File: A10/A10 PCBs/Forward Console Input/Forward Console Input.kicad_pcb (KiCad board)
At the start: 2 copper layers, 99.7 x 98.4 mm, 68 parts, among them J1 PATCH, J10 ROWS, J11 COLUMNS, J12 PATCH, J13 PATCH, J14 PWM, J15 PWM, J16 Communication, J17 PATCH, J18 PATCH, J19 PATCH, J2 FIRE HANDLES, J20 PATCH, J21 Analog, J22 Analog, J23 PATCH, J24 PATCH, J25 Power, J26 Power, J27 Analog, J28 Analog, J29 Digital, J3 UFC COLS, J30 PWM, J31 PWM, J32 Communication, J4 UFC ROWS, J5 PATCH, J6 JAMMER, J7 LANDING GEAR, J8 MASTER ARM, J9 NMSP CMSP, U1 USR-ES1

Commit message: A10
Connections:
- R1 pad 1: /*5 -> /*13
- R2 pad 1: /*6 -> /*12
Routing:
- net GND: track 205.5 -> 0.00 mm
- net /39: track 155.7 -> 0.00 mm
- net /38: track 148.8 -> 0.00 mm
- net /43: track 139.9 -> 0.00 mm, vias 2 -> 0
- net /40: track 139.5 -> 0.00 mm
- net /42: track 122.0 -> 0.00 mm, vias 1 -> 0
- net +5V: track 115.4 -> 0.00 mm
- net /32: track 110.1 -> 0.00 mm, vias 1 -> 0
- net /41: track 107.7 -> 0.00 mm
- net MOSI: track 96.1 -> 0.00 mm
- net /33: track 92.5 -> 0.00 mm, vias 1 -> 0
- net SCLK: track 85.4 -> 0.00 mm
- net /34: track 82.3 -> 0.00 mm, vias 3 -> 0
- net SS: track 80.5 -> 0.00 mm
- net ES1_RST: track 78.1 -> 0.00 mm
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
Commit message: a10
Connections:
- C13 pad 1: /A3 -> /A8
- J2 pad 3: /ROW1O -> /32
- J22 pad 1: /A3 -> /A8
- J28 pad 1: /A3 -> /A8
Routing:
- net GND: track 0.00 -> 214.8 mm
- net /38: track 0.00 -> 154.7 mm
- net /39: track 0.00 -> 153.3 mm, vias 0 -> 1
- net /40: track 0.00 -> 126.4 mm, vias 0 -> 1
- net /41: track 0.00 -> 121.0 mm, vias 0 -> 1
- net /43: track 0.00 -> 119.2 mm, vias 0 -> 3
- net /34: track 0.00 -> 118.3 mm, vias 0 -> 1
- net +5V: track 0.00 -> 116.3 mm
- net /33: track 0.00 -> 100.5 mm, vias 0 -> 2
- net MOSI: track 0.00 -> 97.4 mm
- net /32: track 0.00 -> 94.5 mm
- net /42: track 0.00 -> 94.3 mm, vias 0 -> 1
- net SCLK: track 0.00 -> 84.9 mm
- net SS: track 0.00 -> 80.5 mm
- net ES1_RST: track 0.00 -> 77.6 mm
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
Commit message: A10
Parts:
- J7: footprint Connector_Molex:Molex_KK-254_AE-6410-06A_1x06_P2.54mm_Vertical -> Connector_Molex:Molex_KK-254_AE-6410-08A_1x08_P2.54mm_Vertical
- moved J7 1.37 mm to (193.7, 122.4)
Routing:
- net /37: track 21.8 -> 68.2 mm, vias 0 -> 3
- net /41: track 121.0 -> 153.2 mm
- net /34: track 118.3 -> 89.2 mm, vias 1 -> 3
- net /36: track 56.4 -> 77.0 mm
- net /39: track 153.3 -> 135.5 mm
- net /38: track 154.7 -> 140.5 mm
- net /33: track 100.5 -> 89.2 mm, vias 2 -> 0
- net /*45: track 53.8 -> 62.8 mm, vias 1 -> 2
- net /32: track 94.5 -> 103.4 mm
- net /43: track 119.2 -> 125.4 mm, vias 3 -> 1
- net /28: track 58.7 -> 62.9 mm
- net /22: track 53.9 -> 49.8 mm
- net +5V: track 116.3 -> 120.3 mm, vias 0 -> 2
- net /23: track 50.8 -> 47.2 mm
- net /24: track 47.5 -> 44.1 mm
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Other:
- board text added: "A10 FORWARD CONSOLE VER 1.1"
- board text removed: "A10 FORWARD CONSOLE VER 1.0"

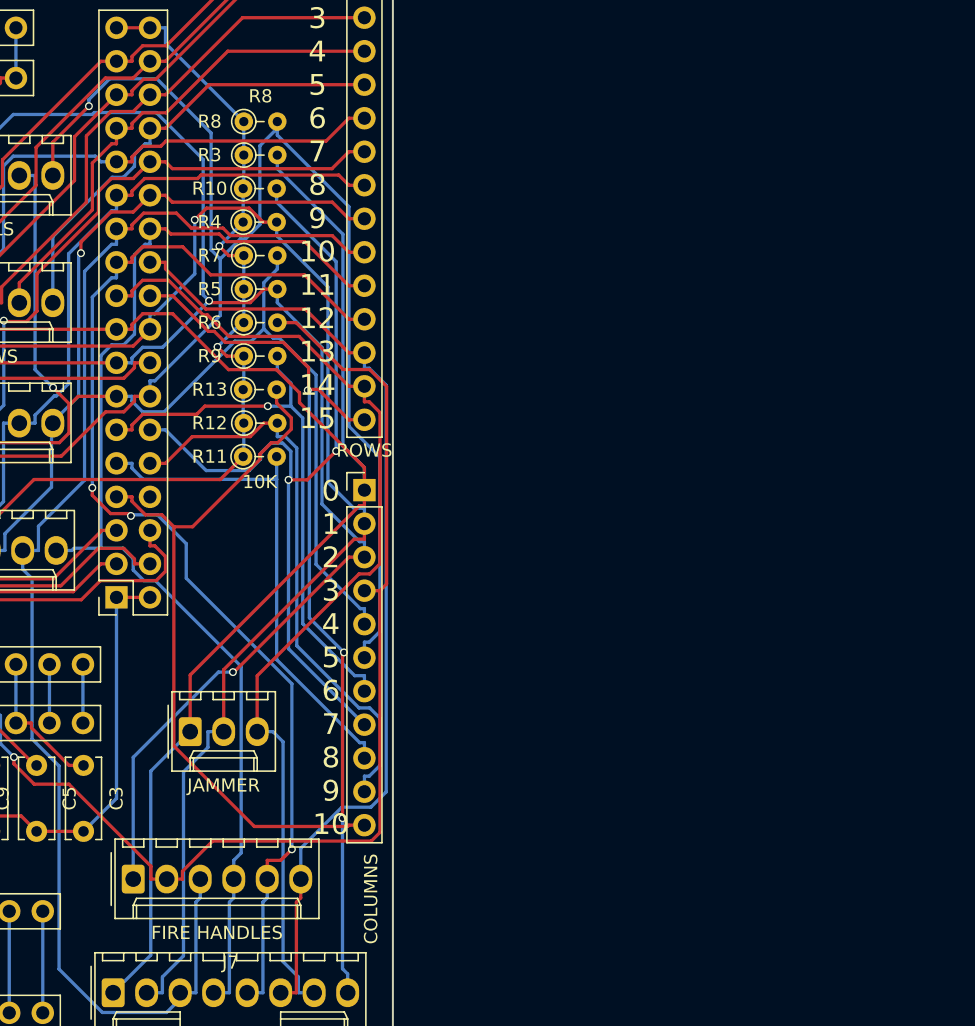
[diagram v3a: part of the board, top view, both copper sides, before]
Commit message: A10 FORWARD INPUT PCB
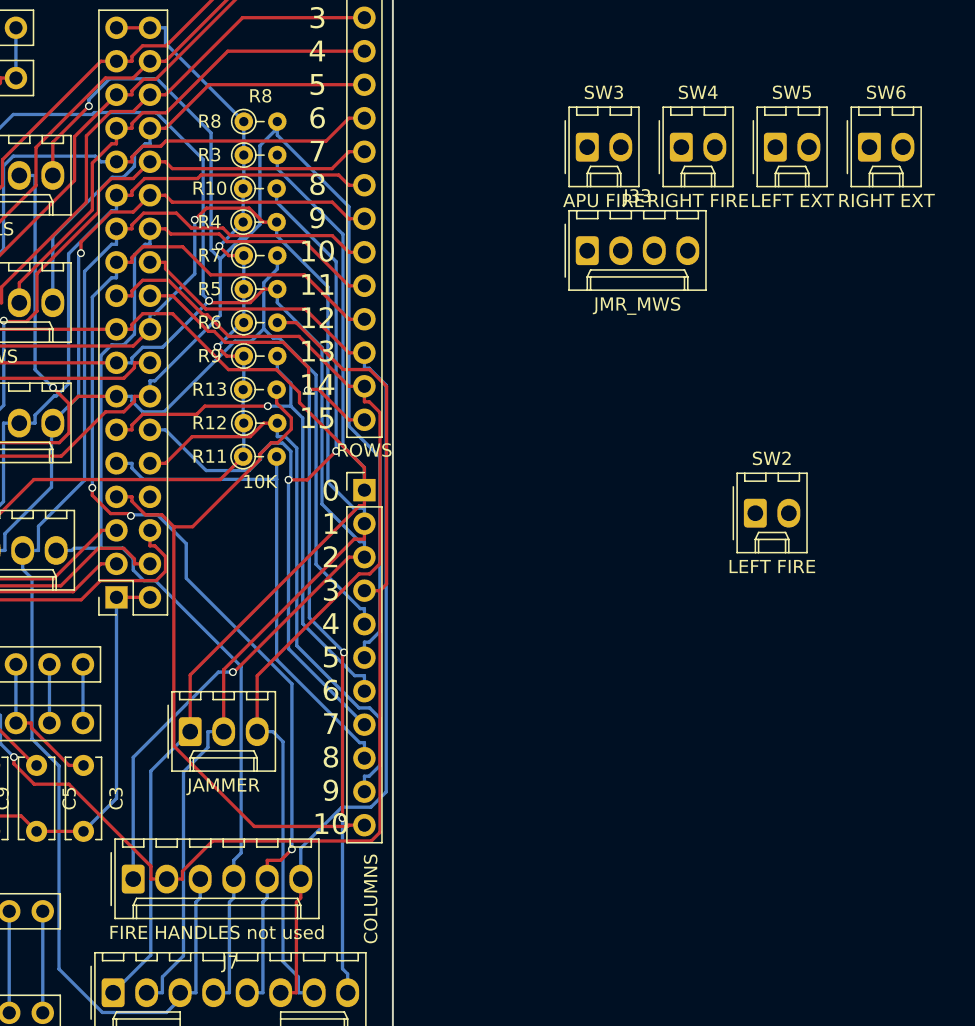
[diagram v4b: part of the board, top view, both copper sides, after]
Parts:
- added J33: JMR_MWS, Connector_Molex:Molex_KK-254_AE-6410-04A_1x04_P2.54mm_Vertical, F.Cu at (229.7, 66.1)
- added SW2: LEFT FIRE, Connector_Molex:Molex_KK-254_AE-6410-02A_1x02_P2.54mm_Vertical, F.Cu at (242.4, 86.0)
- added SW3: APU FIRE, Connector_Molex:Molex_KK-254_AE-6410-02A_1x02_P2.54mm_Vertical, F.Cu at (229.7, 58.2)
- added SW4: RIGHT FIRE, Connector_Molex:Molex_KK-254_AE-6410-02A_1x02_P2.54mm_Vertical, F.Cu at (236.8, 58.2)
- added SW5: LEFT EXT, Connector_Molex:Molex_KK-254_AE-6410-02A_1x02_P2.54mm_Vertical, F.Cu at (243.9, 58.2)
- added SW6: RIGHT EXT, Connector_Molex:Molex_KK-254_AE-6410-02A_1x02_P2.54mm_Vertical, F.Cu at (251.1, 58.2)
- J2: value FIRE HANDLES -> FIRE HANDLES not used
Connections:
- J29 pad 11: /*44 -> unconnected-(J29-Pin_11-Pad11)
- J29 pad 13: /42 -> unconnected-(J29-Pin_13-Pad13)
- J29 pad 27: /28 -> unconnected-(J29-Pin_27-Pad27)
- J29 pad 31: /24 -> unconnected-(J29-Pin_31-Pad31)
- J29 pad 33: /22 -> unconnected-(J29-Pin_33-Pad33)

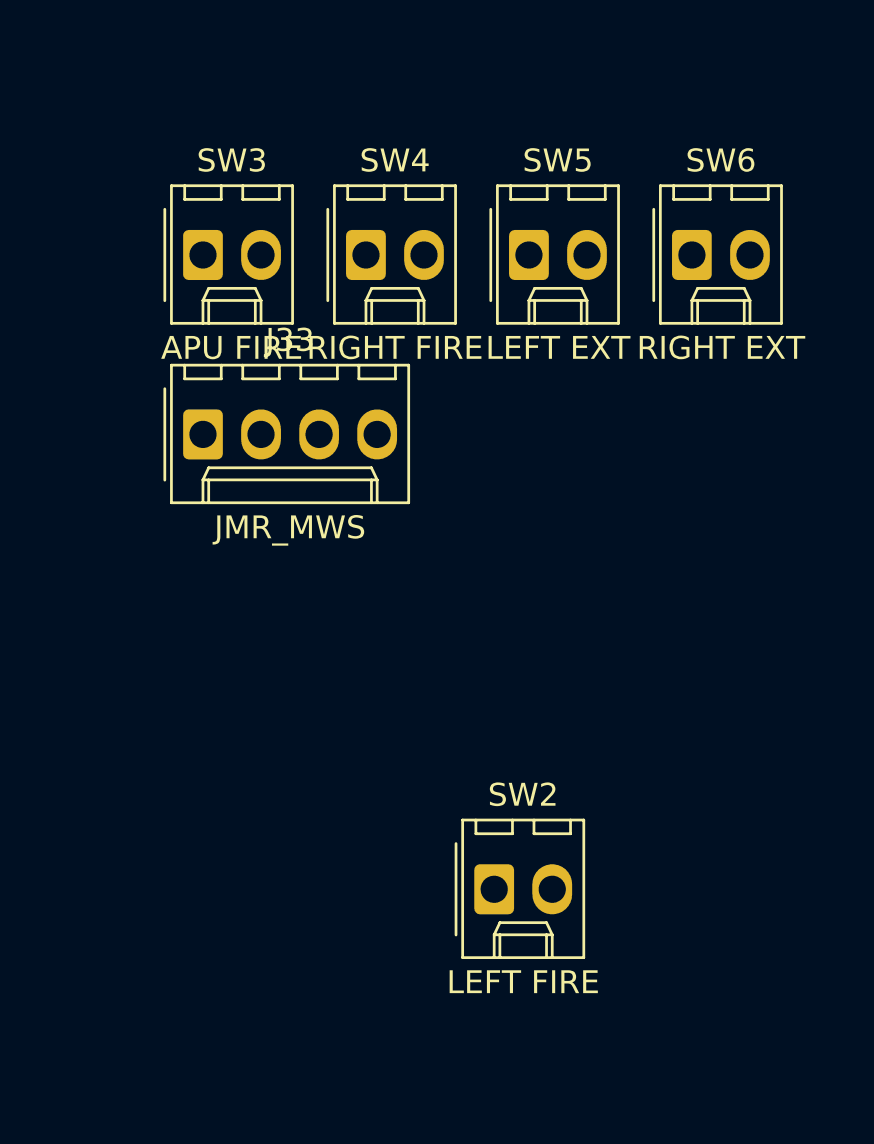
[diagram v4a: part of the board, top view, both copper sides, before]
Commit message: FORWARD CONSOLE INPUT
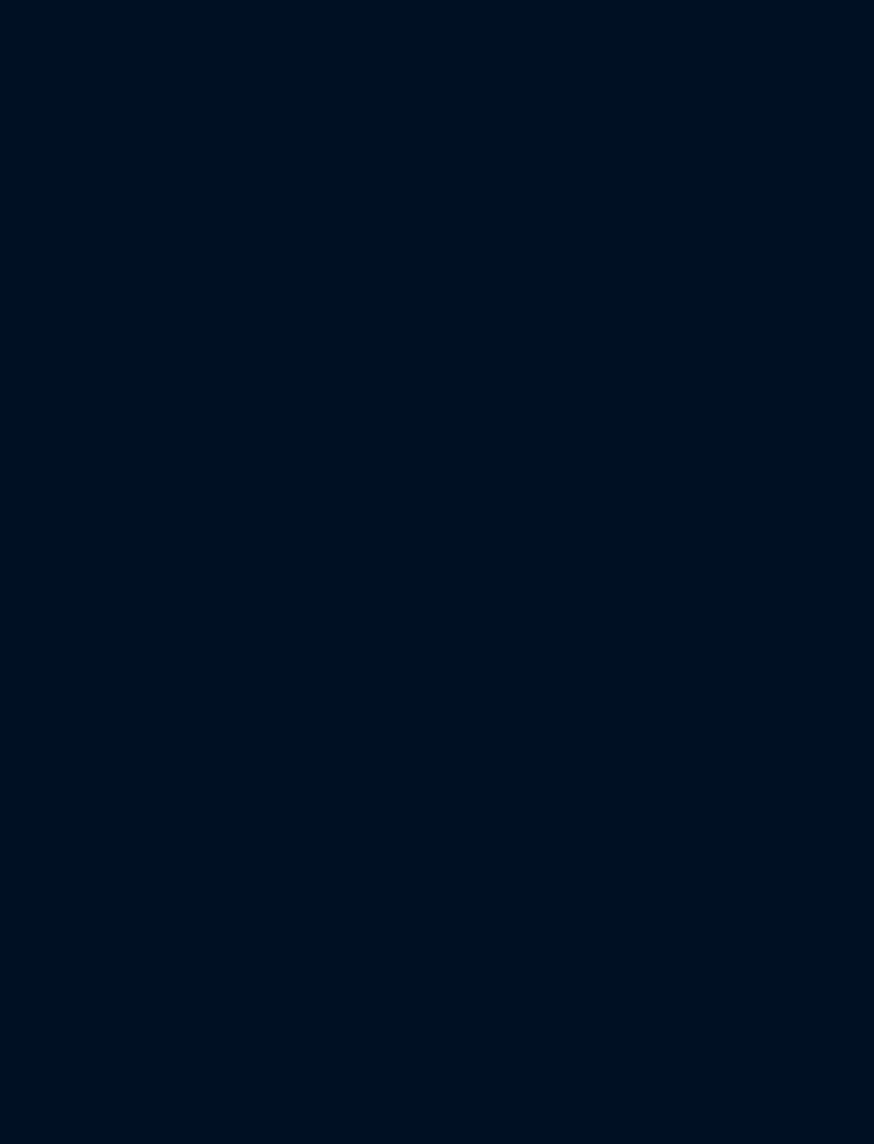
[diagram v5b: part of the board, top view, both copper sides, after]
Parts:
- removed J33: JMR_MWS, Connector_Molex:Molex_KK-254_AE-6410-04A_1x04_P2.54mm_Vertical
- removed SW2: LEFT FIRE, Connector_Molex:Molex_KK-254_AE-6410-02A_1x02_P2.54mm_Vertical
- removed SW3: APU FIRE, Connector_Molex:Molex_KK-254_AE-6410-02A_1x02_P2.54mm_Vertical
- removed SW4: RIGHT FIRE, Connector_Molex:Molex_KK-254_AE-6410-02A_1x02_P2.54mm_Vertical
- removed SW5: LEFT EXT, Connector_Molex:Molex_KK-254_AE-6410-02A_1x02_P2.54mm_Vertical
- removed SW6: RIGHT EXT, Connector_Molex:Molex_KK-254_AE-6410-02A_1x02_P2.54mm_Vertical

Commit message: A10
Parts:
- removed J2: FIRE HANDLES not used, Connector_Molex:Molex_KK-254_AE-6410-06A_1x06_P2.54mm_Vertical
- added D13: D, Diode_THT:D_A-405_P7.62mm_Horizontal, F.Cu at (224.9, 46.1)
- added D14: D, Diode_THT:D_A-405_P7.62mm_Horizontal, F.Cu at (224.9, 50.4)
- added D15: D, Diode_THT:D_A-405_P7.62mm_Horizontal, F.Cu at (224.9, 54.6)
- added D16: D, Diode_THT:D_A-405_P7.62mm_Horizontal, F.Cu at (224.9, 58.9)
- added D17: D, Diode_THT:D_A-405_P7.62mm_Horizontal, F.Cu at (224.9, 63.1)
- added J47: SW LEFT FIRE, Connector_Molex:Molex_KK-254_AE-6410-02A_1x02_P2.54mm_Vertical, F.Cu at (223.9, 80.6)
- added J48: SW APU FIRE, Connector_Molex:Molex_KK-254_AE-6410-02A_1x02_P2.54mm_Vertical, F.Cu at (228.6, 80.6)
- added J49: SW RIGHT FIRE, Connector_Molex:Molex_KK-254_AE-6410-02A_1x02_P2.54mm_Vertical, F.Cu at (242.7, 104.2)
- added J50: FIRE EXT, Connector_Molex:Molex_KK-254_AE-6410-04A_1x04_P2.54mm_Vertical, F.Cu at (237.8, 82.2)
- added R19: 10K, Resistor_THT:R_Axial_DIN0204_L3.6mm_D1.6mm_P2.54mm_Vertical, F.Cu at (237.1, 87.7)
- J11: footprint Connector_PinHeader_2.54mm:PinHeader_1x11_P2.54mm_Vertical -> Connector_PinHeader_2.54mm:PinHeader_1x12_P2.54mm_Vertical
- J6: value JAMMER -> SW JETTISON; footprint Connector_Molex:Molex_KK-254_AE-6410-03A_1x03_P2.54mm_Vertical -> Connector_Molex:Molex_KK-254_AE-6410-02A_1x02_P2.54mm_Vertical
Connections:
- J6 pad 1: /38 -> Net-(D16-K)
- J6 pad 2: /39 -> /35
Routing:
- net GND: track 214.7 -> 0.00 mm
- net /41: track 153.2 -> 0.00 mm, vias 1 -> 0
- net /38: track 140.5 -> 0.00 mm
- net /39: track 135.5 -> 0.00 mm, vias 1 -> 0
- net /43: track 125.4 -> 0.00 mm, vias 1 -> 0
- net /40: track 124.3 -> 0.00 mm, vias 2 -> 0
- net +5V: track 120.3 -> 0.00 mm, vias 2 -> 0
- net /32: track 103.4 -> 0.00 mm
- net MOSI: track 95.7 -> 0.00 mm
- net /42: track 94.5 -> 0.00 mm, vias 1 -> 0
- net /34: track 89.2 -> 0.00 mm, vias 3 -> 0
- net /33: track 89.2 -> 0.00 mm
- net SCLK: track 84.4 -> 0.00 mm
- net SS: track 81.1 -> 0.00 mm
- net ES1_RST: track 78.1 -> 0.00 mm
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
